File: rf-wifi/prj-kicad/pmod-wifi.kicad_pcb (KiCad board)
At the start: 4 copper layers, 38.1 x 20.3 mm, 0 parts

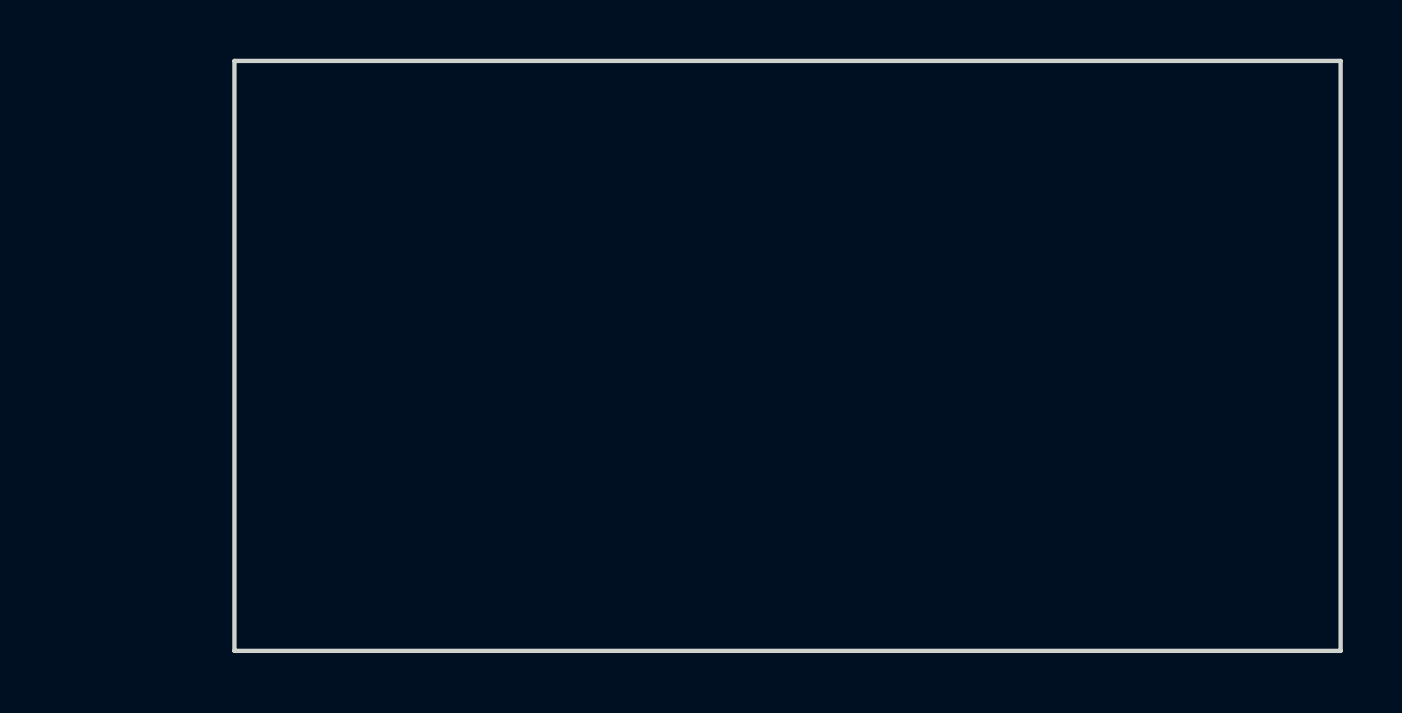
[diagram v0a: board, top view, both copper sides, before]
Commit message: RF-WIFI: Add components footprints and board routing
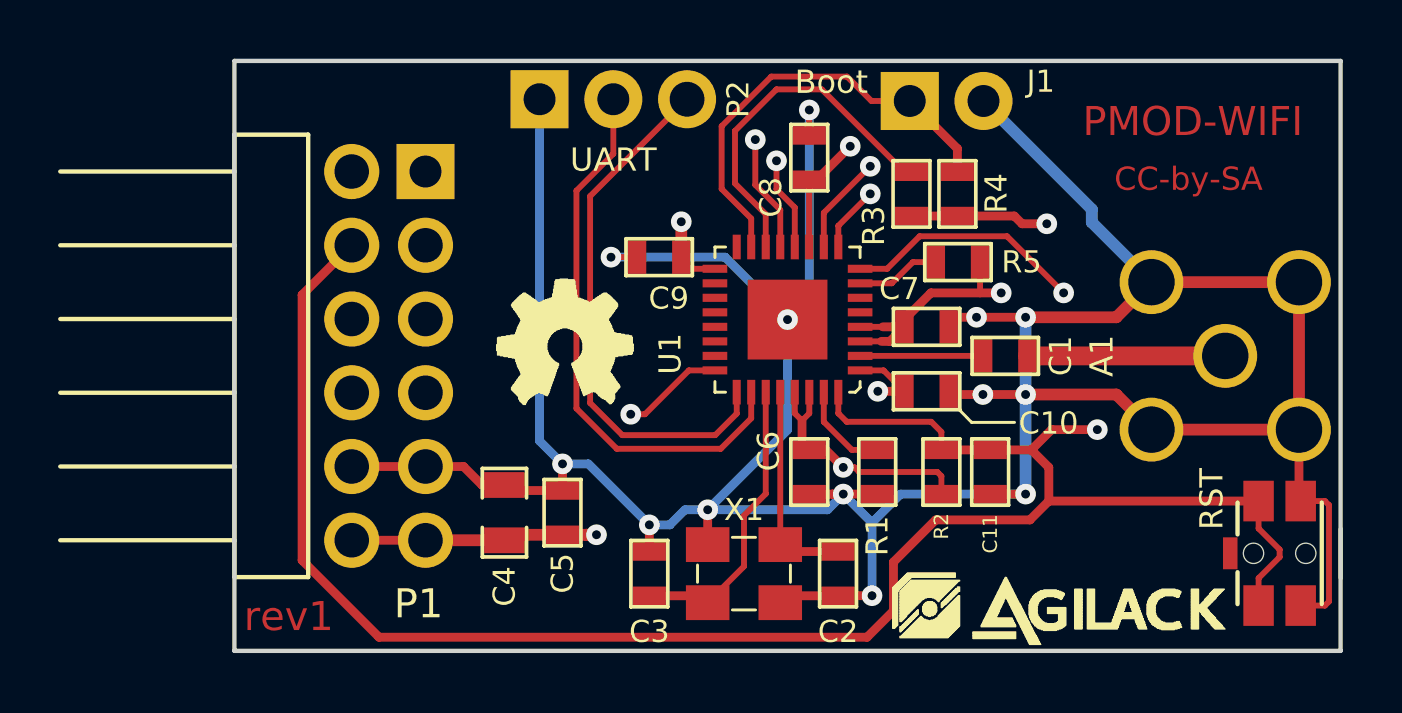
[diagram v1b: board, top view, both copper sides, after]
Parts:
- added A1: ANTENNA, pmod-wifi:CONN_SMA_RA, F.Cu at (163.6, 105.0)
- added C1: 5.6pF, pmod-wifi:SMD0603, F.Cu at (156.0, 105.0)
- added C10: 100nF, pmod-wifi:SMD0603, F.Cu at (153.3, 106.2)
- added C11: 1uF, pmod-wifi:SMD0603, F.Cu at (155.5, 109.0)
- added C2: 10pF, pmod-wifi:SMD0603, F.Cu at (150.2, 112.5)
- added C3: 10pF, pmod-wifi:SMD0603, F.Cu at (143.7, 112.5)
- added C4: 10uF, pmod-wifi:SMD0805, F.Cu at (138.8, 110.4)
- added C5: 100nF, pmod-wifi:SMD0603, F.Cu at (140.8, 110.4)
- added C6: 100nF, pmod-wifi:SMD0603, F.Cu at (149.2, 109.0)
- added C7: 100nF, pmod-wifi:SMD0603, F.Cu at (153.3, 104.0)
- added C8: 100nF, pmod-wifi:SMD0603, F.Cu at (149.2, 98.2)
- added C9: 100nF, pmod-wifi:SMD0603, F.Cu at (144.1, 101.6)
- added J1: JUMPER, pmod-wifi:CONN_2, F.Cu at (154.0, 96.2)
- added LOGO-OHW: VAL**, pmod-wifi:logo-ohw, F.Cu at (140.8, 104.6)
- added P1: PMOD, pmod-wifi:CONN_PMOD-Male, F.Cu at (133.5, 105.0)
- added P2: CONN_3, pmod-wifi:CONN_3, F.Cu at (142.5, 96.2)
- added R1: 12k, pmod-wifi:SMD0603, F.Cu at (151.6, 109.0)
- added R2: 10k, pmod-wifi:SMD0603, F.Cu at (153.8, 109.0)
- added R3: 10k, pmod-wifi:SMD0603, F.Cu at (152.8, 99.4)
- added R4: 10k, pmod-wifi:SMD0603, F.Cu at (154.3, 99.4)
- added R5: 10k, pmod-wifi:SMD0603, F.Cu at (154.4, 101.8)
- added SW1: SW_PUSH, pmod-wifi:SW_PTS840, F.Cu at (165.4, 111.8)
- added U1: ESP8285, pmod-wifi:QFN32, F.Cu at (148.5, 103.8)
- added X1: 26MHz, pmod-wifi:Q_3.2x2.5, F.Cu at (147.0, 112.5)
- added agilack-11.5: 450px, pmod-wifi:logo-agilack-11.5, F.Cu at (158.2, 113.8)
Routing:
- net GND: track 0.00 -> 127.9 mm, vias 0 -> 13
- net +3.3V: track 0.00 -> 86.1 mm, vias 0 -> 7
- net RST: track 0.00 -> 79.0 mm, vias 0 -> 2
- net SPI_INT: track 0.00 -> 21.2 mm, vias 0 -> 1
- net SPI_MISO: track 0.00 -> 20.9 mm, vias 0 -> 1
- net SPI_SCK: track 0.00 -> 20.4 mm, vias 0 -> 1
- net UART_TX: track 0.00 -> 19.1 mm
- net UART_RX: track 0.00 -> 18.4 mm
- net SPI_MOSI: track 0.00 -> 16.5 mm, vias 0 -> 1
- net SPI_CS: track 0.00 -> 15.9 mm, vias 0 -> 1
- net BOOT: track 0.00 -> 15.2 mm
- net /CFG1: track 0.00 -> 12.3 mm
- net Net-(C3-Pad1): track 0.00 -> 10.2 mm
- net Net-(C2-Pad1): track 0.00 -> 7.34 mm
- net Net-(A1-Pad1): track 0.00 -> 6.81 mm
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- added copper zone on In1.Cu, net +3.3V
- added copper zone on B.Cu, net GND
- added copper zone on In1.Cu, net GND
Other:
- board text added: "Boot"
- board text added: "CC-by-SA"
- board text added: "PMOD-WIFI"
- board text added: "RST"
- board text added: "UART"
- board text added: "rev1"

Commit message: RF-WIFI: Add external SPI flash (sch+pcb) for ESP8266 compatibility
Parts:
- added C12: 100nF, pmod-wifi:SMD0603, F.Cu at (159.0, 101.2)
- added U2: M25P16-VME, pmod-wifi:SOIC-8E, F.Cu at (163.5, 98.0)
- moved LOGO-OHW 1.41 mm to (139.5, 105.0)
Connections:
- U1 pad 18: Net-(U1-Pad18) -> MEM_HOLD
- U1 pad 19: Net-(U1-Pad19) -> MEM_WP
- U1 pad 20: Net-(U1-Pad20) -> MEM_CS
- U1 pad 21: Net-(U1-Pad21) -> MEM_CLK
- U1 pad 22: Net-(U1-Pad22) -> MEM_MISO
- U1 pad 23: Net-(U1-Pad23) -> MEM_MOSI
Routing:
- net MEM_WP: track 0.00 -> 31.9 mm, vias 0 -> 2
- net MEM_MISO: track 0.00 -> 31.6 mm, vias 0 -> 2
- net MEM_MOSI: track 0.00 -> 30.4 mm, vias 0 -> 2
- net MEM_CS: track 0.00 -> 28.6 mm, vias 0 -> 2
- net MEM_CLK: track 0.00 -> 27.6 mm, vias 0 -> 2
- net MEM_HOLD: track 0.00 -> 23.2 mm, vias 0 -> 2
- net GND: track 127.9 -> 142.7 mm, vias 13 -> 15
- net +3.3V: track 86.1 -> 89.7 mm
